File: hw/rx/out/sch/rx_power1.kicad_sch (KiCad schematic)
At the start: 14 parts, among them J1 backplane 2x13, U4 TLV75533P, U5 TLV75533P

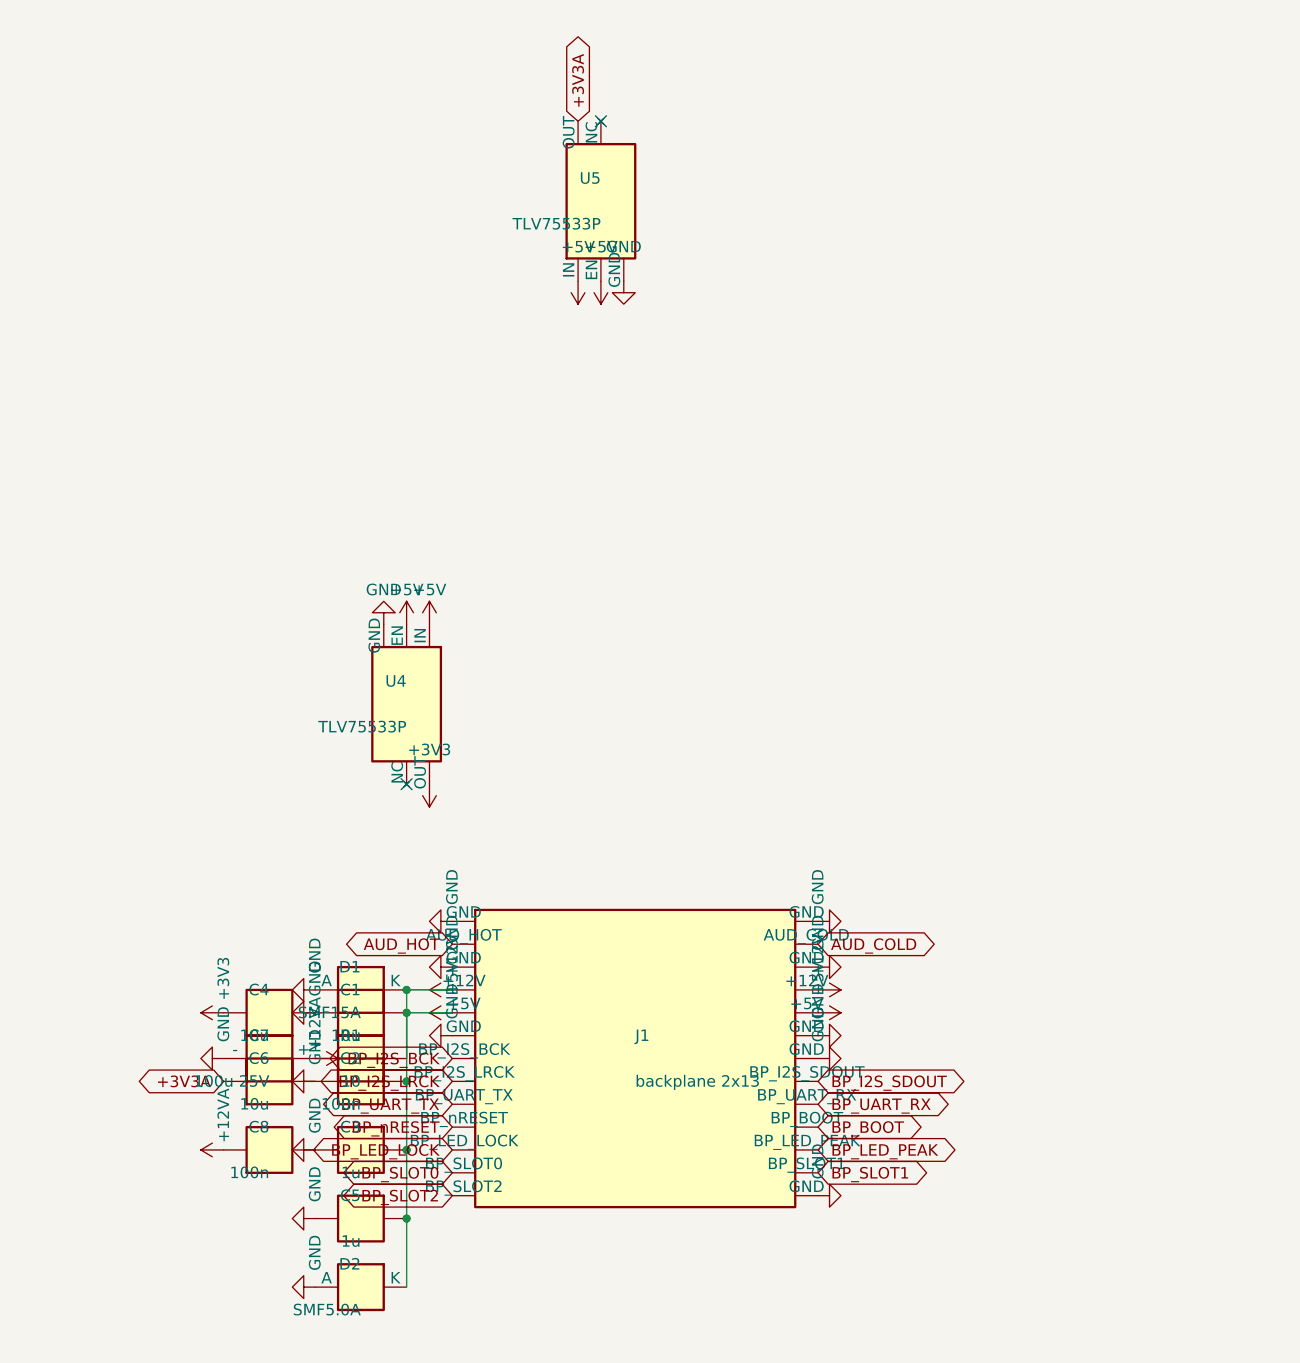
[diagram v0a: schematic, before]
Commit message: hw/rx: review fixes for #81 (mute relay + supervisor, S1J clamps, VCM discharge + 2-pole filter, 16 V LDOs, keyed header, I2S DNP, cable stability + power-cycle SPICE, FLT low latency) (#32)
Co-Authored-By: Claude Opus 5.5 <noreply@anthropic.com>
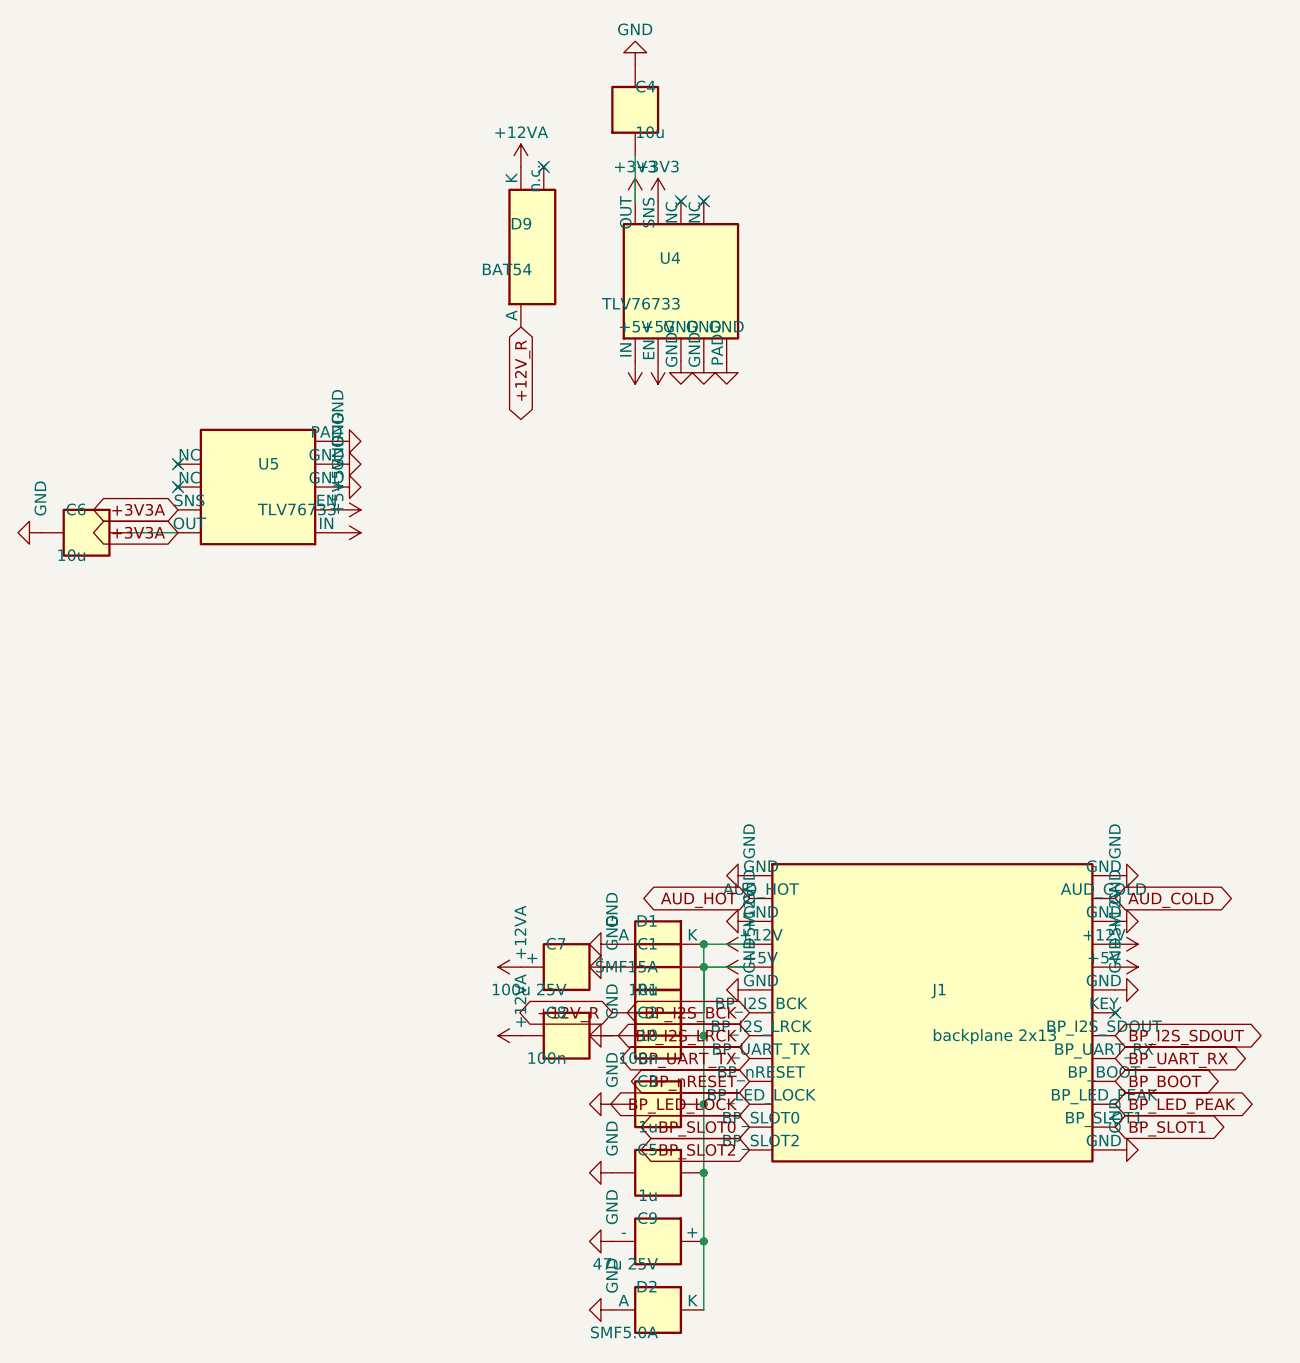
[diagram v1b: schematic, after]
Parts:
- added C9: 47u 25V, Capacitor_SMD:CP_Elec_5x5.4, symbol openpack_rx:CP
- added D9: BAT54, Package_TO_SOT_SMD:SOT-23, symbol openpack_rx:BAT54
- J1: MPN HDR_2x13_2.54_SMD -> HDR_2x13_2.54_SMD_KEY14
- U4, U5: value TLV75533P -> TLV76733; footprint Package_TO_SOT_SMD:SOT-23-5 -> Package_SO:HVSSOP-8-1EP_3x3mm_P0.65mm_EP1.57x1.89mm; symbol openpack_rx:TLV75533P -> openpack_rx:TLV76733; MPN TLV75533PDBVR -> TLV76733DGNR
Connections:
- net +12V: now also U4.5 (EN), U4.8 (IN), U5.5 (EN), U5.8 (IN), C9.1 (+); no longer U4.1 (IN), U4.3 (EN), U5.1 (IN), U5.3 (EN)
- net +12VA: now also D9.3 (K); no longer R1.2
- net +3V3: now also U4.1 (OUT), U4.2 (SNS); no longer U4.5 (OUT)
- net +3V3A: now also U5.1 (OUT), U5.2 (SNS); no longer U5.5 (OUT)
- net GND: now also U4.4 (GND), U4.6 (GND), U4.9 (PAD), U5.4 (GND), U5.6 (GND), U5.9 (PAD), C9.2 (-); no longer J1.14 (GND), U4.2 (GND), U5.2 (GND)
- new net +12V_R: D9.1 (A), R1.2
- no-connect marks 2 -> 6
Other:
- moved on the sheet: C1, C2, C3, C4, C5, C6, C7, C8, D1, D2, R1

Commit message: hw/rx: receiver module BT40NE -> BT40E, FEM node pack-only (ADR-0021, #112)
- hw/rx: BT40E symbol (Fanstel v1.09 p.14 pad map = BT40F/NE names), footprint
  openpack:Fanstel_BT40E (14x16 mm), no FEM nets, P1.05 open; GPIO map unchanged.
  ERC 0/0. BOM: Digi-Key UK GBP 9.7765 q100 -> $30.68 / GBP 23.38 per sub-board.
- fw: receiver builds add boards/role_rx_cpunet.overlay (FEM node disabled, no
  &radio fem); rx.c refuses to build with the FEM enabled.
- ADR-0014 amended (datasheet checks, FCC X8WBT40F, no UKCA DoC, BOM).

Co-Authored-By: Claude Opus 5.5 <noreply@anthropic.com>
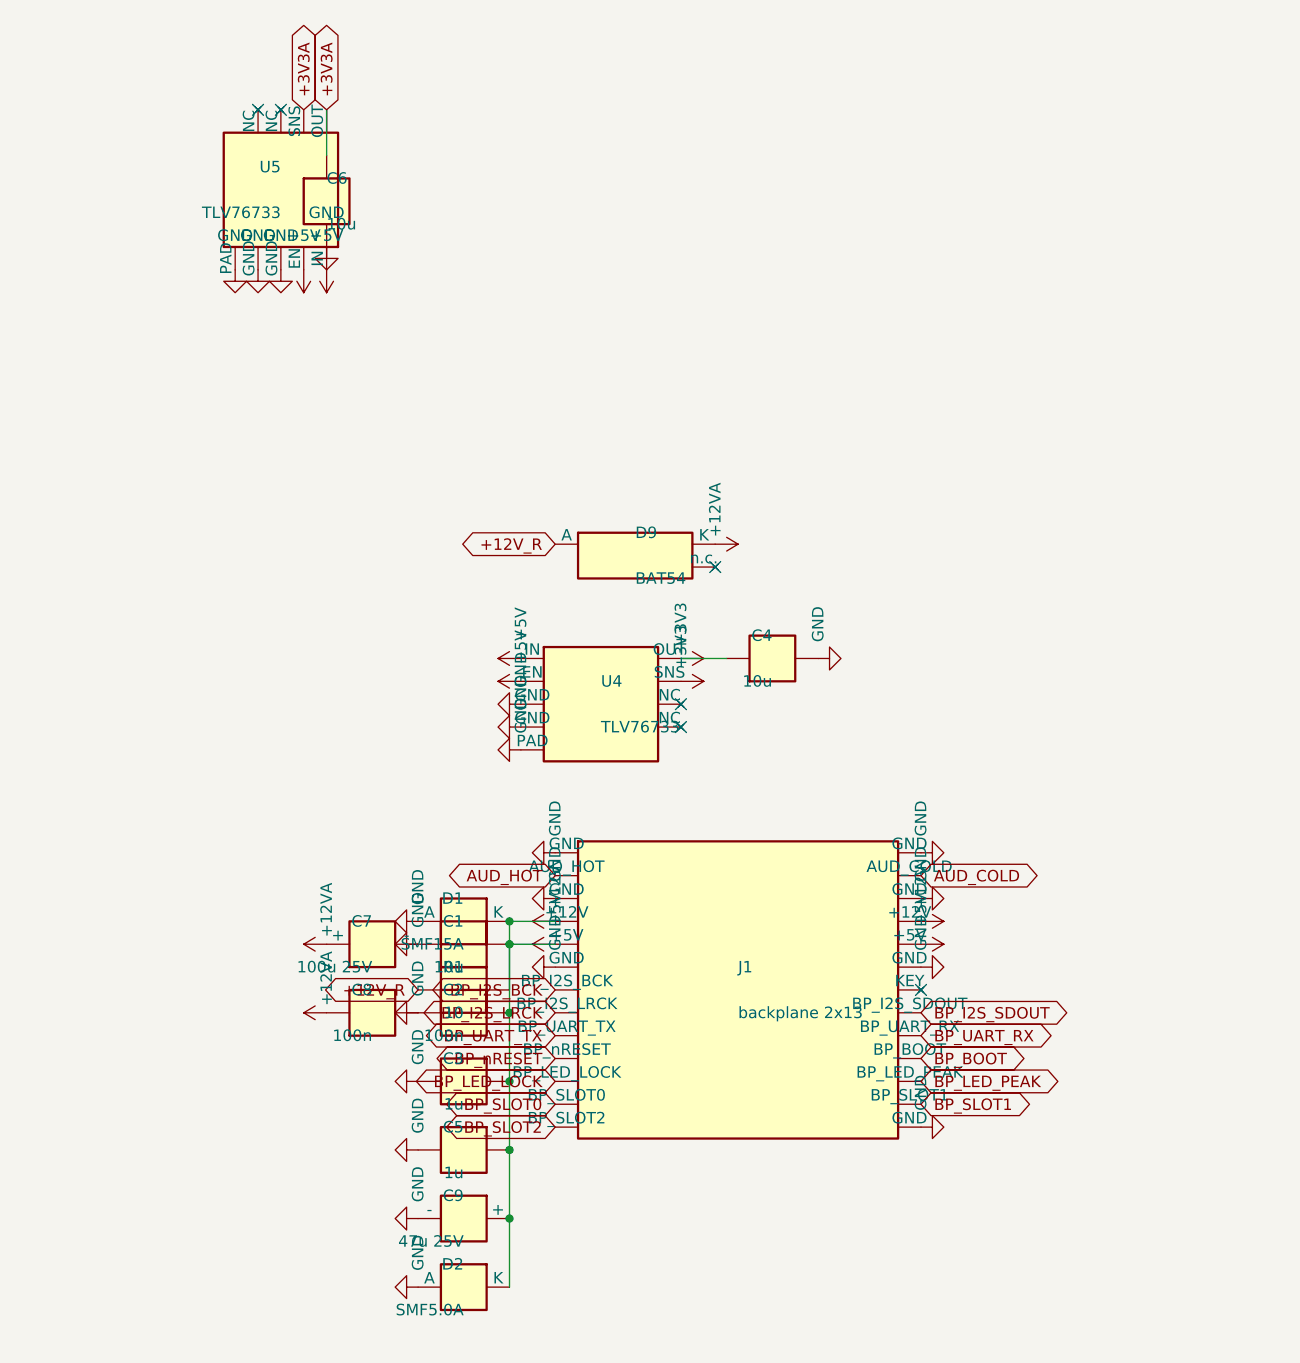
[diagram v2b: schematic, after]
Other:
- moved on the sheet: C1, C2, C3, C4, C5, C6, C7, C8, C9, D1, D2, D9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

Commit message: hw/rx: receiver sub-board layout, 50 ohm GCPW, keyed J1, JLC rules that load, fab outputs (#34) (#116)
Part of #34. Receiver layout (48x90 mm, DRC 0/0), #116 independent-review fixes (netclass pour clearances in rx + pack, no hole at J1 pin 14, solid RF grounds, K1 pin-1/CPL), every placed part with a checked LCSC code.

Co-Authored-By: Claude Opus 5.5 <noreply@anthropic.com>
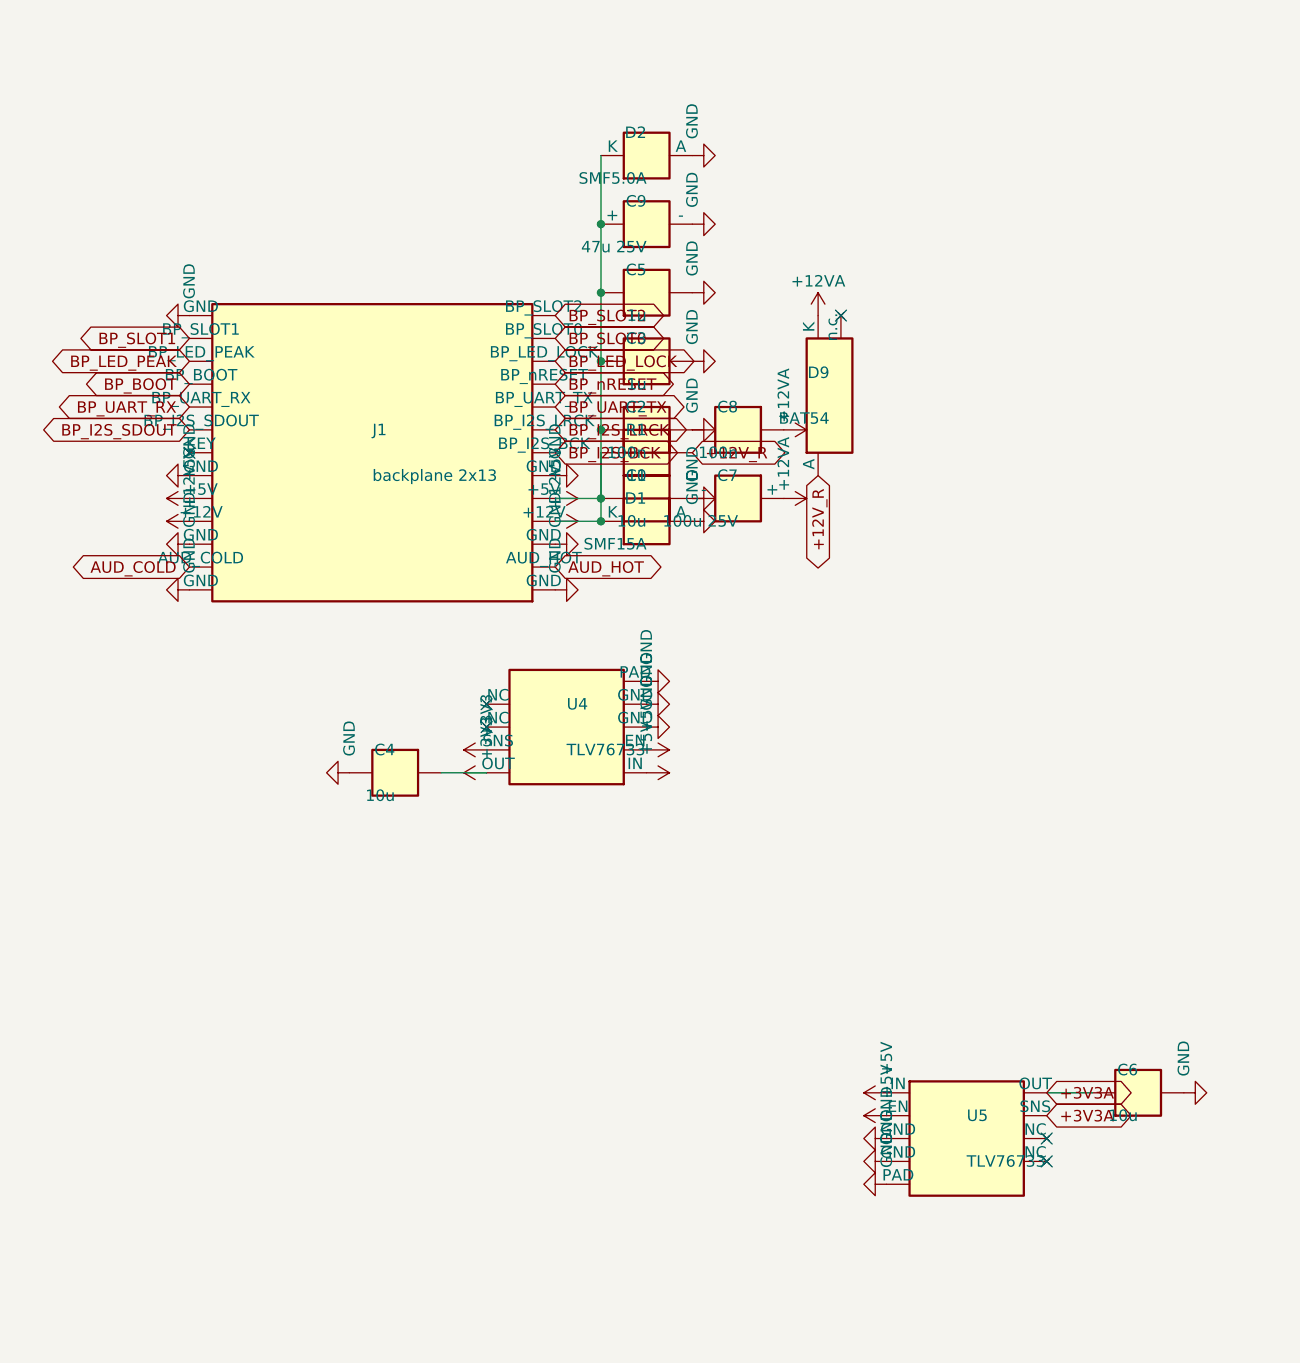
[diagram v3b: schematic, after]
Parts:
- J1: footprint Connector_PinHeader_2.54mm:PinHeader_2x13_P2.54mm_Vertical_SMD -> openpack:PinHeader_2x13_P2.54mm_Key14; MPN HDR_2x13_2.54_SMD_KEY14 -> PZ254V-12-26P
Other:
- moved on the sheet: C1, C2, C3, C4, C5, C6, C7, C8, C9, D1, D2, D9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
